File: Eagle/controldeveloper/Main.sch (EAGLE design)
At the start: 19 parts

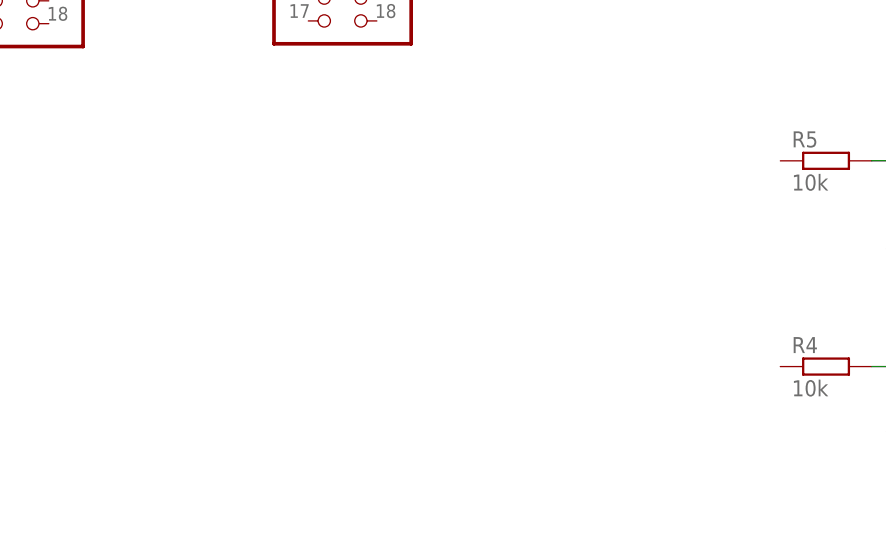
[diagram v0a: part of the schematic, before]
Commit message: Added encoders on Eagle Project
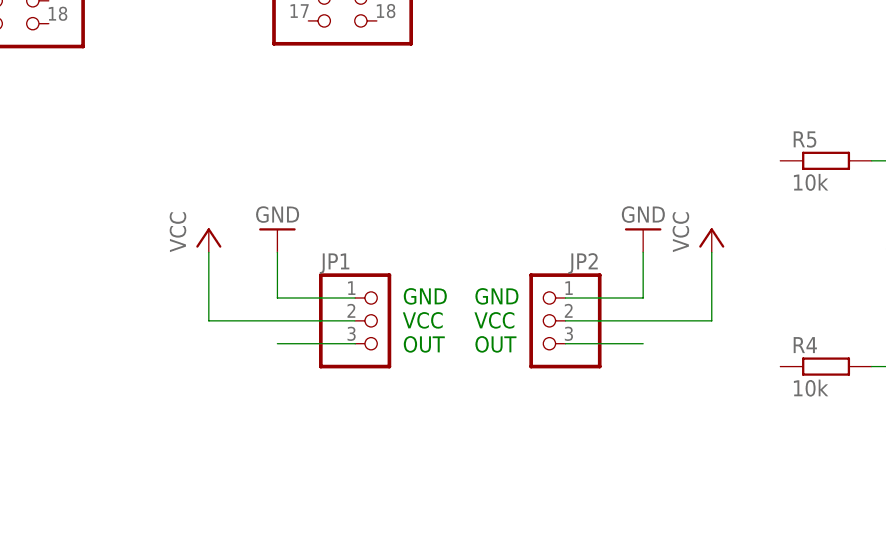
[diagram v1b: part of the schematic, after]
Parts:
- added JP1, JP2: (no value), pinhead:PINHD-1X3/90
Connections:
- new net N$17: JP1.3
- new net N$18: JP2.3
- net GND: now also JP1.1, JP2.1
- net VCC: now also JP1.2, JP2.2
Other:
- note added: "GND VCC OUT"
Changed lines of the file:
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@@
 <part name="P+2" library="supply1" deviceset="VCC" device=""/>
 <part name="P+3" library="supply1" deviceset="VCC" device=""/>
+<part name="JP1" library="pinhead" deviceset="PINHD-1X3" device="/90"/>
+<part name="JP2" library="pinhead" deviceset="PINHD-1X3" device="/90"/>
+<part name="GND11" library="supply1" deviceset="GND" device=""/>
+<part name="GND12" library="supply1" deviceset="GND" device=""/>
+<part name="P+4" library="supply1" deviceset="VCC" device=""/>
+<part name="P+5" library="supply1" deviceset="VCC" device=""/>
 </parts>
 <sheets>
@@
 TX
 GND</text>
+<text x="148.54" y="60" size="1.778" layer="91">GND
+VCC
+OUT</text>
+<text x="156.5" y="60" size="1.778" layer="91">GND
+VCC
+OUT</text>
 </plain>
 <instances>
@@
 <instance part="P+2" gate="VCC" x="76.2" y="119.38"/>
 <instance part="P+3" gate="VCC" x="162.56" y="132.08"/>
+<instance part="JP1" gate="A" x="145.796" y="63.5"/>
+<instance part="JP2" gate="A" x="164.084" y="63.5" rot="MR0"/>
+<instance part="GND11" gate="1" x="134.62" y="73.66" rot="R180"/>
+<instance part="GND12" gate="1" x="175.26" y="73.66" rot="R180"/>
+<instance part="P+4" gate="VCC" x="127" y="73.66"/>
+<instance part="P+5" gate="VCC" x="182.88" y="73.66"/>
 </instances>
 <busses>
@@
 <wire x1="-2.54" y1="99.06" x2="-2.54" y2="96.52" width="0.1524" layer="91"/>
 <pinref part="U3" gate="G$1" pin="GND"/>
+</segment>
+<segment>
+<pinref part="JP1" gate="A" pin="1"/>
+<wire x1="143.256" y1="66.04" x2="134.62" y2="66.04" width="0.1524" layer="91"/>
+<wire x1="134.62" y1="66.04" x2="134.62" y2="71.12" width="0.1524" layer="91"/>
+<pinref part="GND11" gate="1" pin="GND"/>
+</segment>
+<segment>
+<pinref part="JP2" gate="A" pin="1"/>
+<wire x1="166.624" y1="66.04" x2="175.26" y2="66.04" width="0.1524" layer="91"/>
+<wire x1="175.26" y1="66.04" x2="175.26" y2="71.12" width="0.1524" layer="91"/>
+<pinref part="GND12" gate="1" pin="GND"/>
 </segment>
 </net>
@@
 <wire x1="55.88" y1="73.66" x2="55.88" y2="72.58" width="0.1524" layer="91"/>
 </segment>
-</net>
+<segment>
+<pinref part="JP1" gate="A" pin="2"/>
+<wire x1="143.256" y1="63.5" x2="127" y2="63.5" width="0.1524" layer="91"/>
+<wire x1="127" y1="63.5" x2="127" y2="71.12" width="0.1524" layer="91"/>
+<pinref part="P+4" gate="VCC" pin="VCC"/>
+</segment>
+<segment>
+<pinref part="JP2" gate="A" pin="2"/>
+<wire x1="166.624" y1="63.5" x2="182.88" y2="63.5" width="0.1524" layer="91"/>
+<wire x1="182.88" y1="63.5" x2="182.88" y2="71.12" width="0.1524" layer="91"/>
+<pinref part="P+5" gate="VCC" pin="VCC"/>
+</segment>
+</net>
+<net name="N$17" class="0">
+<segment>
+<pinref part="JP1" gate="A" pin="3"/>
+<wire x1="143.256" y1="60.96" x2="134.62" y2="60.96" width="0.1524" layer="91"/>
+</segment>
+</net>
+<net name="N$18" class="0">
+<segment>
+<pinref part="JP2" gate="A" pin="3"/>
+<wire x1="166.624" y1="60.96" x2="175.26" y2="60.96" width="0.1524" layer="91"/>
+</segment>
+</net>

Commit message: Eagle proj - redesigned
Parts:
- removed JP1, JP2: (no value), pinhead:PINHD-1X3/90
- added ENC_R, EN_L: (no value), pinhead:PINHD-1X3
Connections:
- net N$11 renamed VDD
- removed net N$17: JP1.3
- removed net N$18: JP2.3
- removed net N$5: ESP_R.4, RX/TX.1
- removed net N$8: ESP_R.3, R1.1
- new net EN1: ESP_L.8, IN.3
- new net EN2: ESP_L.10, IN.5
- new net ENC_L: EN_L.3, ESP_L.4
- new net ENC_R: ENC_R.3, ESP_R.18
- new net LED1: ESP_R.9, R5.1
- new net LED2: ESP_R.11, R4.1
- new net N$12: ESP_R.5, R1.1
- new net N$14: ESP_R.8, RX/TX.2
- new net PH1: ESP_L.9, IN.4
- new net PH2: ESP_L.7, IN.6
- net GND: now also ENC_R.1, EN_L.1, ESP_R.3; no longer ESP_R.1, JP1.1, JP2.1
- net N$6: now also RX/TX.1; no longer RX/TX.2
- net N$9: now also ESP_R.10; no longer ESP_R.8
- net VCC: now also ENC_R.2, EN_L.2, ESP_R.4; no longer ESP_R.2, JP1.2, JP2.2
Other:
- moved on the sheet: C5, ESP_R, R1, RX/TX

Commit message: Finished eagle board!
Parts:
- removed IC2: (no value), v-reg:LM317TL
- added IC1: (no value), v-reg:LM317TS
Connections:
- removed net N$14: ESP_R.8, RX/TX.2
- removed net N$9: ESP_R.10, RX/TX.3
- new net N$5: ESP_R.4, RX/TX.1
- new net N$8: ESP_R.8, RX/TX.3
- net ENC_R: now also ESP_R.16; no longer ESP_R.18
- net GND: now also ESP_R.1; no longer ESP_R.3
- net LED1: now also ESP_R.7; no longer ESP_R.9
- net LED2: now also ESP_R.9; no longer ESP_R.11
- net N$12: now also ESP_R.3; no longer ESP_R.5
- net N$6: now also RX/TX.2; no longer RX/TX.1
- net N$7: now also IC1.ADJ; no longer IC2.ADJ
- net VCC: now also ESP_R.2, IC1.OUT; no longer ESP_R.4, IC2.OUT
- net VDD: now also IC1.IN; no longer IC2.IN
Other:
- note added: "3.3 TXD RXD GND"
- note added: "GND EN"
- note added: "IO14 IO13"
- note added: "IO16 IO0"
- note added: "IO19 IO5"
- note added: "IO23 IO22"
- note added: "IO27 IO12"
- note added: "IO32 IO25"
- note added: "IO33 IO26"
- note added: "IO4"
- note added: "IO4 IO2"
- note added: "IO5"
- note added: "SD0"
- note added: "SD1"
- note added: "SD2 CMD"
- note added: "SD3 CLK"
- note added: "SVN IO35"
- note added: "SVP IO34"
- moved on the sheet: ESP_L, ESP_R, R1, RX/TX

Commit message: Final version of Eagle board
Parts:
- renumbered RX/TX to GD|RX|TX
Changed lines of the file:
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@@
 <part name="C4" library="resistor" deviceset="C-EU" device="050-025X075" value="10uF"/>
 <part name="GND8" library="supply1" deviceset="GND" device=""/>
-<part name="RX/TX" library="pinhead" deviceset="PINHD-1X3" device=""/>
+<part name="GD|RX|TX" library="pinhead" deviceset="PINHD-1X3" device=""/>
 <part name="LED1" library="led" deviceset="TLLG4400" device=""/>
 <part name="LED2" library="led" deviceset="TLLG4400" device=""/>
@@
 <instance part="C4" gate="G$1" x="76.2" y="106.68"/>
 <instance part="GND8" gate="1" x="76.2" y="96.52"/>
-<instance part="RX/TX" gate="A" x="200.66" y="111.76"/>
+<instance part="GD|RX|TX" gate="A" x="200.66" y="111.76"/>
 <instance part="LED1" gate="G$1" x="205.74" y="73.66"/>
 <instance part="LED2" gate="G$1" x="205.74" y="53.34"/>
@@
 </segment>
 <segment>
+<pinref part="ESP_R" gate="A" pin="2"/>
 <pinref part="P+3" gate="VCC" pin="VCC"/>
-<pinref part="ESP_R" gate="A" pin="2"/>
 <wire x1="165.1" y1="116.84" x2="180.34" y2="116.84" width="0.1524" layer="91"/>
 <wire x1="180.34" y1="116.84" x2="180.34" y2="127" width="0.1524" layer="91"/>
@@
 <wire x1="180.34" y1="127" x2="180.34" y2="129.54" width="0.1524" layer="91"/>
 <wire x1="167.64" y1="127" x2="180.34" y2="127" width="0.1524" layer="91"/>
+<junction x="180.34" y="127"/>
 </segment>
 </net>
@@
 </net>
 <net name="VDD" class="0">
-<segment>
-<wire x1="17.78" y1="109.22" x2="17.78" y2="116.84" width="0.1524" layer="91"/>
-<pinref part="SUPPLY1" gate="G$1" pin="VDD"/>
-<pinref part="U3" gate="G$1" pin="VBUS"/>
-<pinref part="C5" gate="G$1" pin="+"/>
-<wire x1="-5.08" y1="109.22" x2="7.62" y2="109.22" width="0.1524" layer="91"/>
-<wire x1="7.62" y1="111.76" x2="7.62" y2="109.22" width="0.1524" layer="91"/>
-<wire x1="7.62" y1="109.22" x2="17.78" y2="109.22" width="0.1524" layer="91"/>
-</segment>
 <segment>
 <wire x1="43.18" y1="111.76" x2="38.1" y2="111.76" width="0.1524" layer="91"/>
@@
 <pinref part="SUPPLY3" gate="G$1" pin="VDD"/>
 </segment>
+<segment>
+<pinref part="U3" gate="G$1" pin="VBUS"/>
+<pinref part="C5" gate="G$1" pin="+"/>
+<wire x1="-5.08" y1="109.22" x2="7.62" y2="109.22" width="0.1524" layer="91"/>
+<wire x1="7.62" y1="109.22" x2="7.62" y2="111.76" width="0.1524" layer="91"/>
+<pinref part="SUPPLY1" gate="G$1" pin="VDD"/>
+<wire x1="7.62" y1="109.22" x2="17.78" y2="109.22" width="0.1524" layer="91"/>
+<wire x1="17.78" y1="109.22" x2="17.78" y2="116.84" width="0.1524" layer="91"/>
+<junction x="7.62" y="109.22"/>
+</segment>
 </net>
 <net name="N$5" class="0">
 <segment>
-<pinref part="RX/TX" gate="A" pin="1"/>
+<pinref part="GD|RX|TX" gate="A" pin="1"/>
 <pinref part="ESP_R" gate="A" pin="4"/>
 <wire x1="198.12" y1="114.3" x2="165.1" y2="114.3" width="0.1524" layer="91"/>
@@
 <segment>
 <pinref part="ESP_R" gate="A" pin="6"/>
-<pinref part="RX/TX" gate="A" pin="2"/>
+<pinref part="GD|RX|TX" gate="A" pin="2"/>
 <wire x1="165.1" y1="111.76" x2="198.12" y2="111.76" width="0.1524" layer="91"/>
 </segment>
@@
 <net name="N$8" class="0">
 <segment>
-<pinref part="RX/TX" gate="A" pin="3"/>
+<pinref part="GD|RX|TX" gate="A" pin="3"/>
 <pinref part="ESP_R" gate="A" pin="8"/>
 <wire x1="198.12" y1="109.22" x2="165.1" y2="109.22" width="0.1524" layer="91"/>

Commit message: **** **First RELEASE** ****
Fully working version of code and Eagle design!
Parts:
- R4, R5: value 10k -> 0.6k
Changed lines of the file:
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@@
 <part name="LED1" library="led" deviceset="TLLG4400" device=""/>
 <part name="LED2" library="led" deviceset="TLLG4400" device=""/>
-<part name="R4" library="rcl" deviceset="R-EU_" device="0207/10" value="10k"/>
-<part name="R5" library="rcl" deviceset="R-EU_" device="0207/10" value="10k"/>
+<part name="R4" library="rcl" deviceset="R-EU_" device="0207/10" value="0.6k"/>
+<part name="R5" library="rcl" deviceset="R-EU_" device="0207/10" value="0.6k"/>
 <part name="GND9" library="supply1" deviceset="GND" device=""/>
 <part name="GND10" library="supply1" deviceset="GND" device=""/>

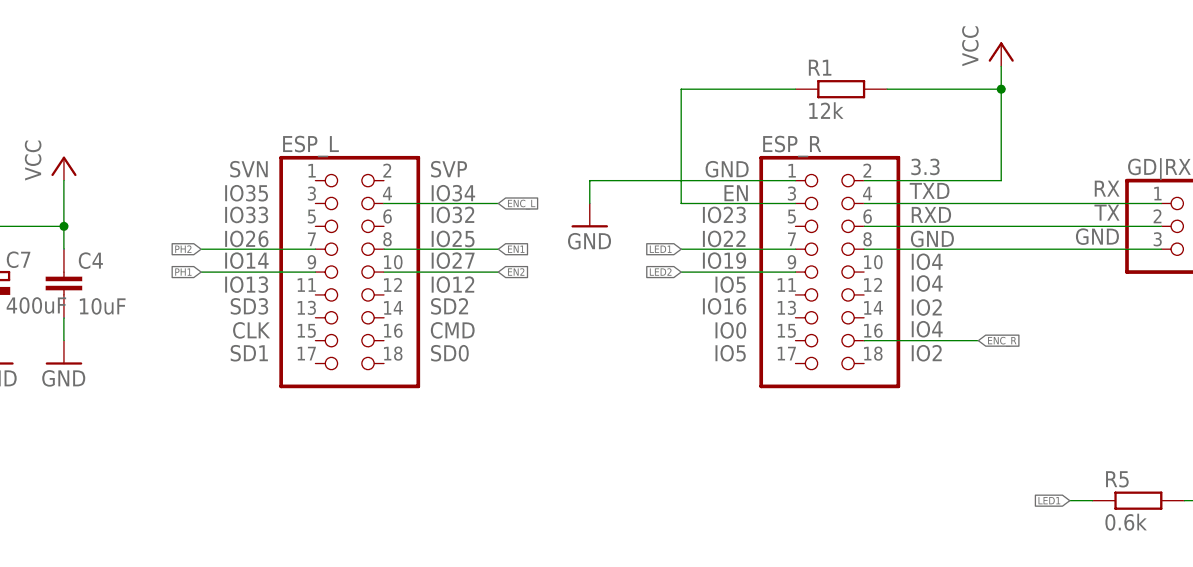
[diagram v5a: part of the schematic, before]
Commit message: ****Release*** NO MORE Radio bugs
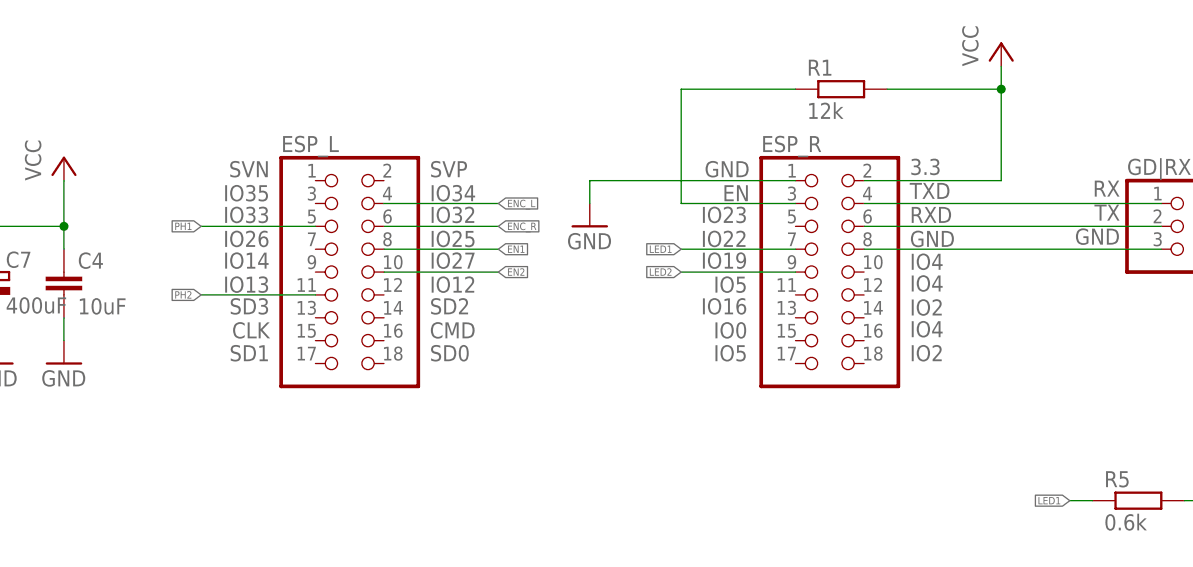
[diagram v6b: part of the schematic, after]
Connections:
- net ENC_R: now also ESP_L.6; no longer ESP_R.16
- net PH1: now also ESP_L.5; no longer ESP_L.9
- net PH2: now also ESP_L.11; no longer ESP_L.7
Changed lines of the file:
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@@
 <net name="ENC_R" class="0">
 <segment>
-<label x="177.8" y="99.06" size="0.8128" layer="95" xref="yes"/>
-<pinref part="ESP_R" gate="A" pin="16"/>
-<wire x1="177.8" y1="99.06" x2="165.1" y2="99.06" width="0.1524" layer="91"/>
+<label x="124.46" y="111.76" size="0.8128" layer="95" xref="yes"/>
+<pinref part="ESP_L" gate="A" pin="6"/>
+<wire x1="111.76" y1="111.76" x2="124.46" y2="111.76" width="0.1524" layer="91"/>
 </segment>
 <segment>
@@
 </segment>
 <segment>
-<pinref part="ESP_L" gate="A" pin="9"/>
-<wire x1="104.14" y1="106.68" x2="91.44" y2="106.68" width="0.1524" layer="91"/>
-<label x="91.44" y="106.68" size="0.8128" layer="95" rot="R180" xref="yes"/>
+<label x="91.44" y="111.76" size="0.8128" layer="95" rot="R180" xref="yes"/>
+<pinref part="ESP_L" gate="A" pin="5"/>
+<wire x1="104.14" y1="111.76" x2="91.44" y2="111.76" width="0.1524" layer="91"/>
 </segment>
 </net>
@@
 </segment>
 <segment>
-<pinref part="ESP_L" gate="A" pin="7"/>
-<wire x1="104.14" y1="109.22" x2="91.44" y2="109.22" width="0.1524" layer="91"/>
-<label x="91.44" y="109.22" size="0.8128" layer="95" rot="R180" xref="yes"/>
+<label x="91.44" y="104.14" size="0.8128" layer="95" rot="R180" xref="yes"/>
+<pinref part="ESP_L" gate="A" pin="11"/>
+<wire x1="104.14" y1="104.14" x2="91.44" y2="104.14" width="0.1524" layer="91"/>
 </segment>
 </net>

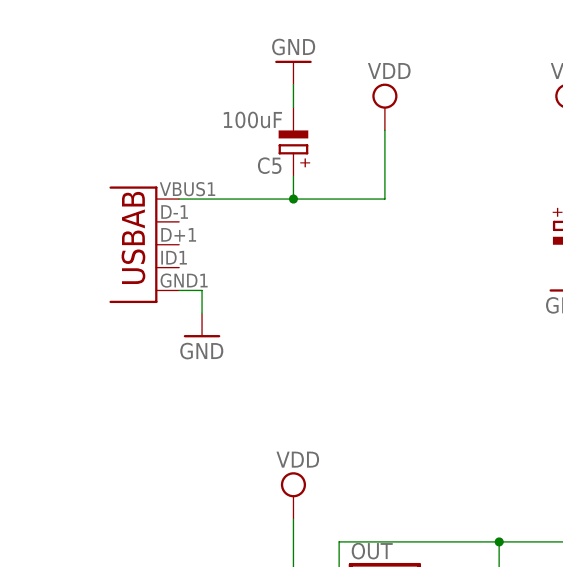
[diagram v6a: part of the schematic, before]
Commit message: Eagle PCB Redesigned
* Routes were optimized
* Space for heat sink added
* Added Power ON/OFF switch
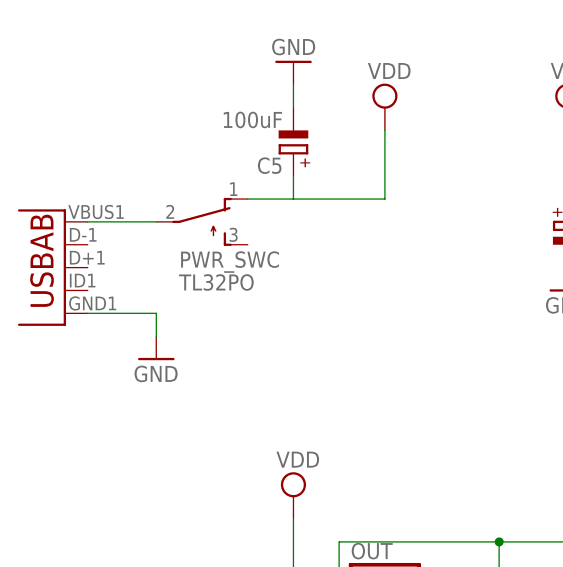
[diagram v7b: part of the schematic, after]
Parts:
- added PWR_SWC: TL32PO, switch:TL32PO
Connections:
- new net N$11: PWR_SWC.P, U3.VBUS
- net VDD: now also PWR_SWC.O; no longer U3.VBUS
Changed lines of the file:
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@@
 <part name="ENC_R" library="pinhead" deviceset="PINHD-1X3" device=""/>
 <part name="IC1" library="v-reg" deviceset="LM317TS" device=""/>
+<part name="PWR_SWC" library="switch" deviceset="TL32PO" device=""/>
 </parts>
 <sheets>
@@
 <instance part="C6" gate="G$1" x="38.1" y="106.68"/>
 <instance part="C7" gate="G$1" x="68.58" y="106.68"/>
-<instance part="GND2" gate="1" x="-2.54" y="93.98"/>
+<instance part="GND2" gate="1" x="-7.62" y="91.44"/>
 <instance part="GND5" gate="1" x="7.62" y="124.46" rot="R180"/>
-<instance part="U3" gate="G$1" x="-10.16" y="104.14" rot="R180"/>
+<instance part="U3" gate="G$1" x="-20.32" y="101.6" rot="R180"/>
 <instance part="ESP_L" gate="A" x="106.68" y="106.68"/>
 <instance part="P+1" gate="VCC" x="55.88" y="76.2"/>
@@
 <instance part="ENC_R" gate="A" x="137.16" y="55.88" rot="MR0"/>
 <instance part="IC1" gate="1" x="50.8" y="111.76"/>
+<instance part="PWR_SWC" gate="BEF1" x="-2.54" y="106.68" rot="R270"/>
 </instances>
 <busses>
@@
 <segment>
 <pinref part="GND2" gate="1" pin="GND"/>
-<wire x1="-5.08" y1="99.06" x2="-2.54" y2="99.06" width="0.1524" layer="91"/>
-<wire x1="-2.54" y1="99.06" x2="-2.54" y2="96.52" width="0.1524" layer="91"/>
+<wire x1="-15.24" y1="96.52" x2="-7.62" y2="96.52" width="0.1524" layer="91"/>
+<wire x1="-7.62" y1="96.52" x2="-7.62" y2="93.98" width="0.1524" layer="91"/>
 <pinref part="U3" gate="G$1" pin="GND"/>
 </segment>
@@
 </segment>
 <segment>
-<pinref part="U3" gate="G$1" pin="VBUS"/>
 <pinref part="C5" gate="G$1" pin="+"/>
-<wire x1="-5.08" y1="109.22" x2="7.62" y2="109.22" width="0.1524" layer="91"/>
 <wire x1="7.62" y1="109.22" x2="7.62" y2="111.76" width="0.1524" layer="91"/>
 <pinref part="SUPPLY1" gate="G$1" pin="VDD"/>
 <wire x1="7.62" y1="109.22" x2="17.78" y2="109.22" width="0.1524" layer="91"/>
 <wire x1="17.78" y1="109.22" x2="17.78" y2="116.84" width="0.1524" layer="91"/>
-<junction x="7.62" y="109.22"/>
+<pinref part="PWR_SWC" gate="BEF1" pin="O"/>
+<wire x1="2.54" y1="109.22" x2="7.62" y2="109.22" width="0.1524" layer="91"/>
 </segment>
 </net>
@@
 </segment>
 </net>
+<net name="N$11" class="0">
+<segment>
+<pinref part="U3" gate="G$1" pin="VBUS"/>
+<pinref part="PWR_SWC" gate="BEF1" pin="P"/>
+<wire x1="-15.24" y1="106.68" x2="-7.62" y2="106.68" width="0.1524" layer="91"/>
+</segment>
+</net>
